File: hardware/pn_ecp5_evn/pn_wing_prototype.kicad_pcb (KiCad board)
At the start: 4 copper layers, 129.5 x 52.2 mm, 260 parts, among them J101 Screw_Terminal_01x02, J102 Conn_Coaxial, J103 Conn_02x20_Odd_Even, J104 Conn_Coaxial, J105 Conn_Coaxial, J106 Conn_Coaxial, J107 Conn_01x10, J201 Conn_Coaxial, J301 Conn_Coaxial, J401 Conn_Coaxial, J601 Conn_Coaxial, J701 Conn_Coaxial, J702 Conn_Coaxial, J703 Conn_Coaxial, U201 VEMI65AB-HCI, U202 LMX2594, U301 PAT1220-C-3DB, U302 TRF37A73, U303 PAT1220-C-3DB, U401 PAT1220-C-3DB, U402 TRF37A73, U403 PAT1220-C-3DB, U501 LM27761, U502 ADM7171ACPZ-3.3-R7, U503 TPS72301DB, U601 LM2904, U602 OPA2211, U701 SYM-63LH+, U702 ADG621, U703 OPA2211, U801 THS4551, U802 LT6657BHMS8-2.5, U901 ADS7868, U902 ADS7868, U903 Si8640BB-B-IU, U904 Si8640BB-B-IU, U905 Si8642BB-B-IU, X601 ABLNO

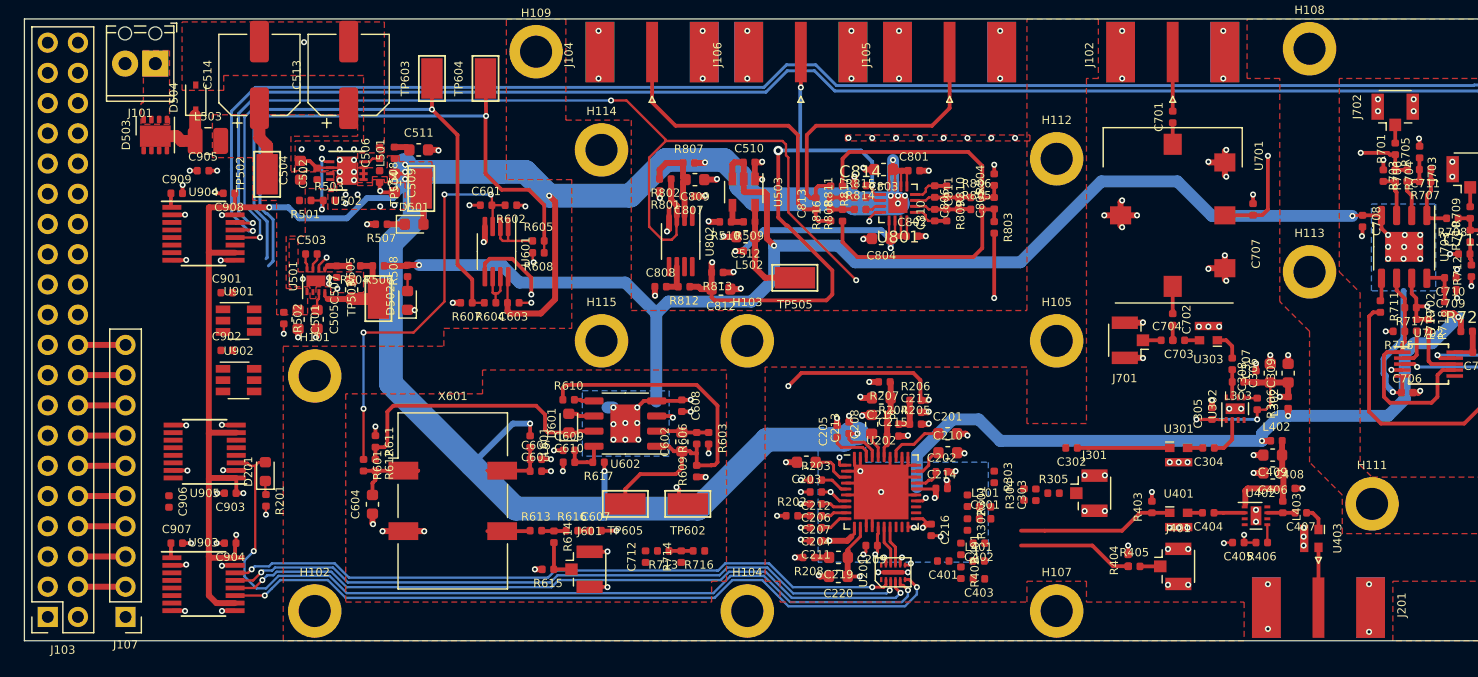
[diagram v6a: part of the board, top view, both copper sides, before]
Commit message: all nets connected in layout
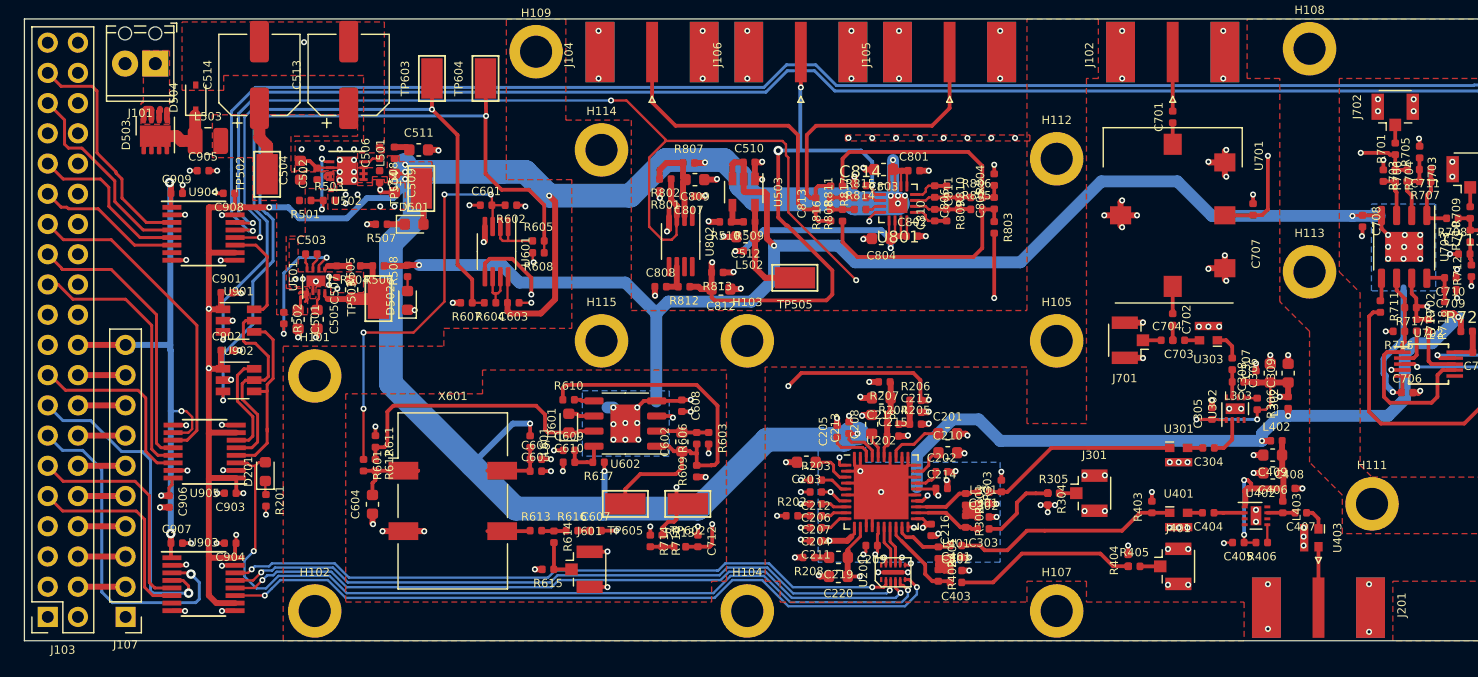
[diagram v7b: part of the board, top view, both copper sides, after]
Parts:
- moved C302 8.27 mm to (110.6, 105.5)
- moved C303 5.26 mm to (110.6, 108.6), turned to 180 degrees
- moved C712 4.59 mm to (86.6, 109.6), turned to 270 degrees
- moved R716 3.20 mm to (83.6, 109.6), turned to 270 degrees
- moved R714 2.92 mm to (82.6, 109.6), turned to 270 degrees
- moved R304 2.03 mm to (116.0, 106.1), turned to 270 degrees
- moved C403 1.95 mm to (108.3, 113.1)
- moved C402 1.94 mm to (108.3, 110.0)
- moved R401 1.93 mm to (106.8, 110.6)
- moved L401 1.92 mm to (108.3, 111.0)
- moved R402 1.91 mm to (106.8, 112.5)
- moved R713 1.44 mm to (85.1, 110.1), turned to 0 degrees
- moved C401 1.34 mm to (108.3, 112.1), turned to 0 degrees
- moved R303 0.97 mm to (112.1, 105.0), turned to 90 degrees
- moved L301 0.29 mm to (110.6, 106.5)
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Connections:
- J103 pad 11: /isolator/LMX_SCK -> /isolator/LMX_SDI
- J103 pad 13: /isolator/LMX_CS -> /isolator/LMX_CE
- J103 pad 15: /isolator/LMX_SDI -> /isolator/LMX_SCK
- J103 pad 23: /isolator/SYNTH_VT_CS -> /isolator/ADC_SCK
- J103 pad 25: /isolator/REF_VT_CS -> /isolator/ADC_SDO
- J103 pad 27: /isolator/ADC_SCK -> /isolator/SYNTH_VT_CS
- J103 pad 29: /isolator/ADC_SDO -> /isolator/REF_VT_CS
- J103 pad 9: /isolator/LMX_CE -> /isolator/LMX_CS
- U905 pad 12: /isolator/ADC_SCK -> /isolator/ADC_SDO
- U905 pad 13: /isolator/ADC_SDO -> /isolator/ADC_SCK
- U905 pad 4: /isolator/ADC_SDO_ISO -> /isolator/ADC_SCK_ISO
- U905 pad 5: /isolator/ADC_SCK_ISO -> /isolator/ADC_SDO_ISO
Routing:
- net +3.3VP: track 6.47 -> 50.1 mm, vias 0 -> 4
- net /isolator/LMX_CE: track 0.00 -> 28.8 mm, vias 0 -> 1
- net /isolator/SYNTH_VT_CS: track 0.00 -> 27.2 mm
- net /isolator/LMX_SCK: track 0.00 -> 27.0 mm, vias 0 -> 1
- net /isolator/ADC_SDO: track 0.00 -> 23.6 mm
- net /isolator/ADC_SCK: track 0.00 -> 22.6 mm
- net /isolator/IF_G1: track 0.00 -> 19.7 mm
- net /isolator/LMX_SDI: track 0.00 -> 19.0 mm
- net /isolator/LMX_CS: track 0.00 -> 17.2 mm
- net /isolator/IF_G2: track 0.00 -> 17.1 mm
- net /isolator/ADC_SDO_ISO: track 0.00 -> 16.7 mm
- net /isolator/LMX_MUXOUT: track 0.00 -> 16.2 mm
- net /isolator/ADC_SCK_ISO: track 0.00 -> 15.1 mm
- net /isolator/BUF_~PD: track 0.00 -> 13.9 mm
- net /VT_REF_TLM: track 49.9 -> 63.8 mm, vias 1 -> 2
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
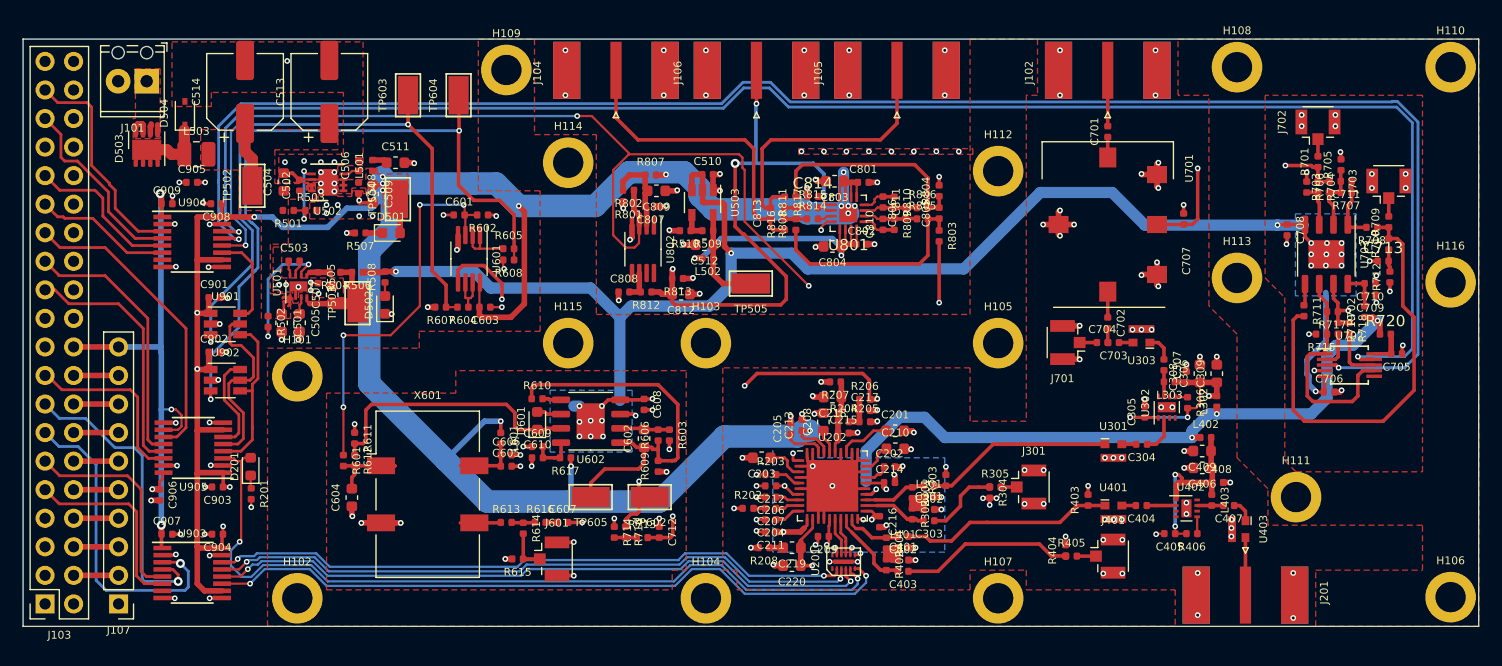
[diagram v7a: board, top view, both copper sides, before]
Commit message: finished silkscreen cleanup, added via stitching
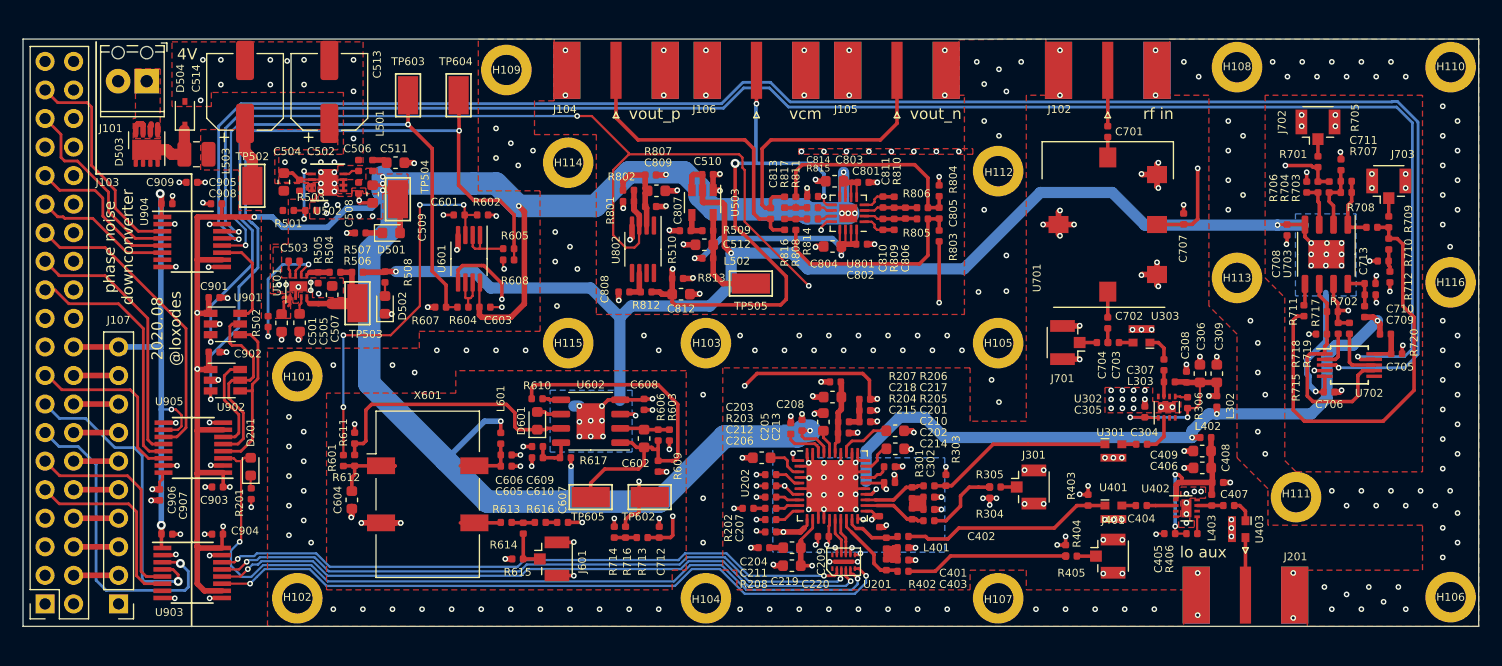
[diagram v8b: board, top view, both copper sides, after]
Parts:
- added G***: LOGO, vna:cat, B.Cu at (77.4, 105.8)
- moved C604 0.21 mm to (59.2, 106.8)
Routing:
- net GND: track 155.1 -> 156.7 mm, vias 206 -> 398
- net Net-(C403-Pad1): track 15.4 -> 14.5 mm
- net +3V3: vias 28 -> 27
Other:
- board text added: "2020.08 @loxodes"
- board text added: "4V"
- board text added: "lo aux"
- board text added: "phase noise downconverter"
- board text added: "rf in"
- board text added: "vcm"
- board text added: "vout_n"
- board text added: "vout_p"
